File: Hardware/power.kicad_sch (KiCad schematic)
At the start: 13 parts, among them J2 USB_C_Receptacle, U3 ADP2164ACPZ-3.3-R7

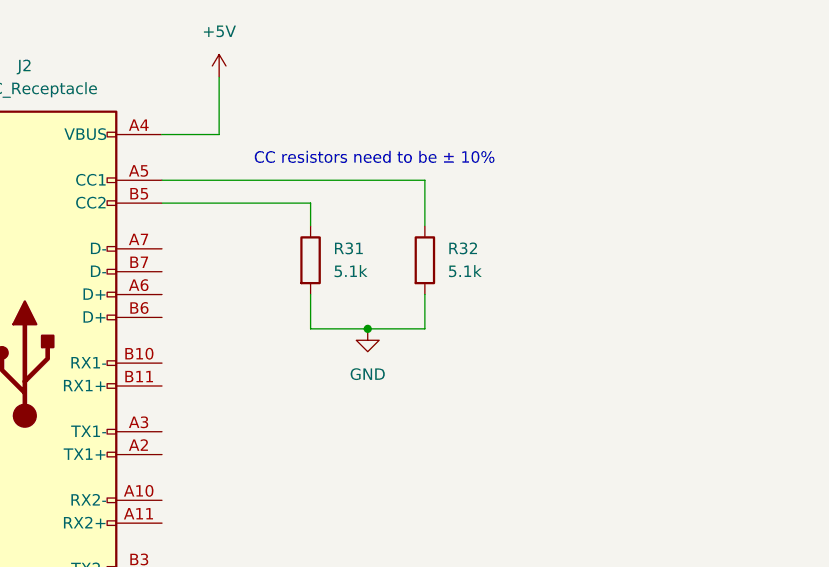
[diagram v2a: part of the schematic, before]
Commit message: connected USB 2.0 data pins
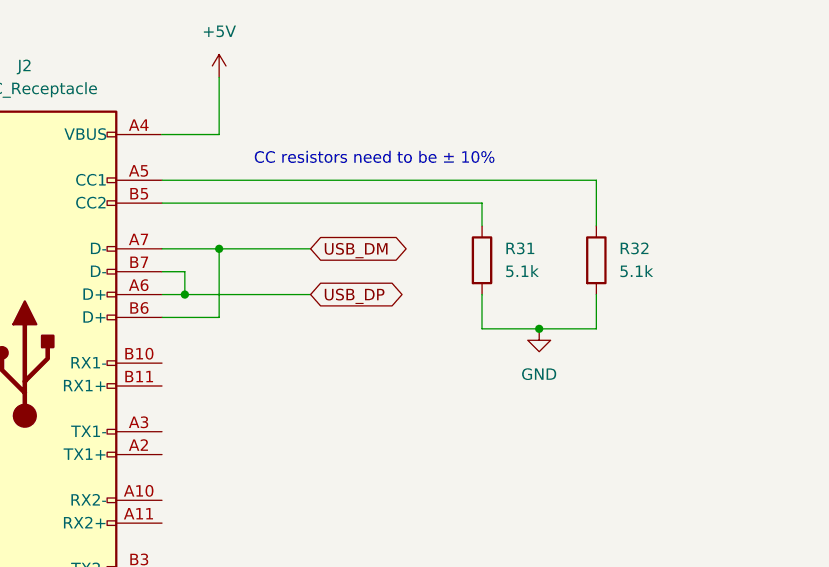
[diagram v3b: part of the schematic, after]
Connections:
- net USB_DP: now reaches J2.A6 (D+)
- net USB_DP: now also J2.B7 (D-)
- net USB_DM: now reaches J2.A7 (D-)
- net USB_DM: now also J2.B6 (D+)
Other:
- moved on the sheet: R31, R32
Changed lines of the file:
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@@
 	)
 	(junction
+		(at 102.87 134.62)
+		(diameter 0)
+		(color 0 0 0 0)
+	)
+	(junction
 		(at 66.04 40.64)
 		(diameter 0)
@@
 	)
 	(junction
+		(at 106.68 129.54)
+		(diameter 0)
+		(color 0 0 0 0)
+	)
+	(junction
 		(at 44.45 40.64)
 		(diameter 0)
@@
 	)
 	(junction
-		(at 123.19 138.43)
+		(at 142.24 138.43)
 		(diameter 0)
 		(color 0 0 0 0)
@@
 	(wire
 		(pts
+			(xy 106.68 137.16) (xy 106.68 129.54)
+		)
+		(stroke
+			(width 0)
+			(type default)
+		)
+	)
+	(wire
+		(pts
 			(xy 68.58 43.18) (xy 66.04 43.18)
 		)
@@
 	(wire
 		(pts
+			(xy 100.33 132.08) (xy 102.87 132.08)
+		)
+		(stroke
+			(width 0)
+			(type default)
+		)
+	)
+	(wire
+		(pts
 			(xy 27.94 35.56) (xy 27.94 40.64)
 		)
@@
 	(wire
 		(pts
+			(xy 102.87 132.08) (xy 102.87 134.62)
+		)
+		(stroke
+			(width 0)
+			(type default)
+		)
+	)
+	(wire
+		(pts
 			(xy 68.58 36.83) (xy 66.04 36.83)
 		)
@@
 	(wire
 		(pts
-			(xy 129.54 134.62) (xy 129.54 138.43)
+			(xy 148.59 134.62) (xy 148.59 138.43)
 		)
 		(stroke
@@
 	(wire
 		(pts
-			(xy 116.84 134.62) (xy 116.84 138.43)
+			(xy 135.89 134.62) (xy 135.89 138.43)
 		)
 		(stroke
@@
 	(wire
 		(pts
+			(xy 106.68 129.54) (xy 116.84 129.54)
+		)
+		(stroke
+			(width 0)
+			(type default)
+		)
+	)
+	(wire
+		(pts
 			(xy 151.13 34.29) (xy 151.13 30.48)
 		)
@@
 	(wire
 		(pts
+			(xy 102.87 134.62) (xy 116.84 134.62)
+		)
+		(stroke
+			(width 0)
+			(type default)
+		)
+	)
+	(wire
+		(pts
 			(xy 104.14 87.63) (xy 107.95 87.63)
 		)
@@
 	(wire
 		(pts
-			(xy 129.54 138.43) (xy 123.19 138.43)
+			(xy 148.59 138.43) (xy 142.24 138.43)
 		)
 		(stroke
@@
 	(wire
 		(pts
-			(xy 116.84 124.46) (xy 116.84 127)
+			(xy 135.89 124.46) (xy 135.89 127)
 		)
 		(stroke
@@
 	(wire
 		(pts
-			(xy 129.54 121.92) (xy 129.54 127)
+			(xy 148.59 121.92) (xy 148.59 127)
 		)
 		(stroke
@@
 	(wire
 		(pts
+			(xy 100.33 134.62) (xy 102.87 134.62)
+		)
+		(stroke
+			(width 0)
+			(type default)
+		)
+	)
+	(wire
+		(pts
 			(xy 66.04 52.07) (xy 68.58 52.07)
 		)
@@
 	(wire
 		(pts
-			(xy 116.84 138.43) (xy 123.19 138.43)
+			(xy 135.89 138.43) (xy 142.24 138.43)
 		)
 		(stroke
@@
 	(wire
 		(pts
+			(xy 106.68 129.54) (xy 100.33 129.54)
+		)
+		(stroke
+			(width 0)
+			(type default)
+		)
+	)
+	(wire
+		(pts
 			(xy 107.95 87.63) (xy 107.95 90.17)
 		)
@@
 	(wire
 		(pts
-			(xy 100.33 121.92) (xy 129.54 121.92)
+			(xy 100.33 121.92) (xy 148.59 121.92)
+		)
+		(stroke
+			(width 0)
+			(type default)
+		)
+	)
+	(wire
+		(pts
+			(xy 100.33 137.16) (xy 106.68 137.16)
 		)
 		(stroke
@@
 	(wire
 		(pts
-			(xy 100.33 124.46) (xy 116.84 124.46)
+			(xy 100.33 124.46) (xy 135.89 124.46)
 		)
 		(stroke
@@
 		)
 	)
+	(global_label "USB_DP"
+		(shape bidirectional)
+		(at 116.84 134.62 0)
+		(fields_autoplaced yes)
+		(effects
+			(font
+				(size 1.27 1.27)
+			)
+			(justify left)
+		)
+		(property "Intersheetrefs" "${INTERSHEET_REFS}"
+			(at 127.1428 134.62 0)
+			(effects
+				(font
+					(size 1.27 1.27)
+				)
+				(justify left)
+				(hide yes)
+			)
+		)
+	)
+	(global_label "USB_DM"
+		(shape bidirectional)
+		(at 116.84 129.54 0)
+		(fields_autoplaced yes)
+		(effects
+			(font
+				(size 1.27 1.27)
+			)
+			(justify left)
+		)
+		(property "Intersheetrefs" "${INTERSHEET_REFS}"
+			(at 127.3242 129.54 0)
+			(effects
+				(font
+					(size 1.27 1.27)
+				)
+				(justify left)
+				(hide yes)
+			)
+		)
+	)
 	(symbol
 		(lib_id "TRME337K010R0035:TRME337K010R0035")
@@
 	(symbol
 		(lib_id "power:GND")
-		(at 123.19 138.43 0)
+		(at 142.24 138.43 0)
 		(unit 1)
 		(exclude_from_sim no)
@@
 		(fields_autoplaced yes)
 		(property "Reference" "#PWR026"
-			(at 123.19 144.78 0)
+			(at 142.24 144.78 0)
 			(effects
 				(font
@@
 		)
 		(property "Value" "GND"
-			(at 123.19 143.51 0)
+			(at 142.24 143.51 0)
 			(effects
 				(font
@@
 		)
 		(property "Footprint" ""
-			(at 123.19 138.43 0)
+			(at 142.24 138.43 0)
 			(effects
 				(font
@@
 		)
 		(property "Datasheet" ""
-			(at 123.19 138.43 0)
+			(at 142.24 138.43 0)
 			(effects
 				(font
@@
 		)
 		(property "Description" "Power symbol creates a global label with name \"GND\" , ground"
-			(at 123.19 138.43 0)
+			(at 142.24 138.43 0)
 			(effects
 				(font
@@
 	(symbol
 		(lib_id "Device:R")
-		(at 116.84 130.81 0)
+		(at 135.89 130.81 0)
 		(unit 1)
 		(exclude_from_sim no)
@@
 		(fields_autoplaced yes)
 		(property "Reference" "R31"
-			(at 119.38 129.5399 0)
+			(at 138.43 129.5399 0)
 			(effects
 				(font
@@
 		)
 		(property "Value" "5.1k"
-			(at 119.38 132.0799 0)
+			(at 138.43 132.0799 0)
 			(effects
 				(font
@@
 		)
 		(property "Footprint" "Resistor_SMD:R_0402_1005Metric"
-			(at 115.062 130.81 90)
+			(at 134.112 130.81 90)
 			(effects
 				(font
@@
 		)
 		(property "Datasheet" "~"
-			(at 116.84 130.81 0)
+			(at 135.89 130.81 0)
 			(effects
 				(font
@@
 		)
 		(property "Description" "Resistor"
-			(at 116.84 130.81 0)
+			(at 135.89 130.81 0)
 			(effects
 				(font
@@
 	(symbol
 		(lib_id "Device:R")
-		(at 129.54 130.81 0)
+		(at 148.59 130.81 0)
 		(unit 1)
 		(exclude_from_sim no)
@@
 		(fields_autoplaced yes)
 		(property "Reference" "R32"
-			(at 132.08 129.5399 0)
+			(at 151.13 129.5399 0)
 			(effects
 				(font
@@
 		)
 		(property "Value" "5.1k"
-			(at 132.08 132.0799 0)
+			(at 151.13 132.0799 0)
 			(effects
 				(font
@@
 		)
 		(property "Footprint" "Resistor_SMD:R_0402_1005Metric"
-			(at 127.762 130.81 90)
+			(at 146.812 130.81 90)
 			(effects
 				(font
@@
 		)
 		(property "Datasheet" "~"
-			(at 129.54 130.81 0)
+			(at 148.59 130.81 0)
 			(effects
 				(font
@@
 		)
 		(property "Description" "Resistor"
-			(at 129.54 130.81 0)
+			(at 148.59 130.81 0)
 			(effects
 				(font
